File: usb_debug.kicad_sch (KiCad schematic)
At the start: 12 parts, among them J10 DBG pads (SWCLK SWDIO GND), J4 USB_C_PROGRAM_POWER

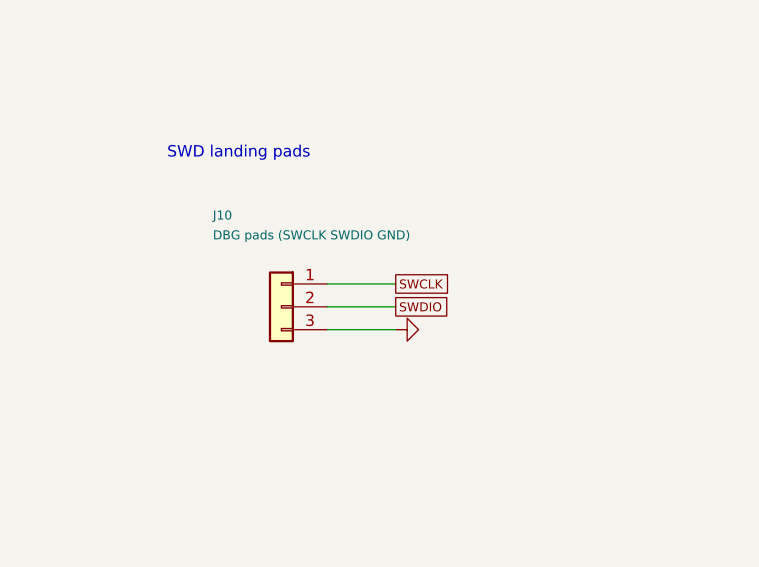
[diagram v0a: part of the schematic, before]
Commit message: Order-ready: core regulator per RP2350 §6.3.8, SWD header, second DVDD cap, README rewrite
Core regulator (U20 / C39 / C45 / L20):
- C39/C45 lands narrowed to 0.46 mm (0.50 mm gap) so VREG_LX passes between
  the pads as in datasheet Fig. 23; local 0.12 mm clearance rule for those
  two footprints only (inside JLC's 3.5 mil four-layer tier)
- In1 GND cutout under L20 and the LX net (Fig. 24); single-point ground
  return with two adjacent vias; B.Cu GND pour tying the SD-cluster vias
- L20 switched to the polarity-marked Abracon AOTA-B201610S3R3-101-T
  (LCSC C42411119) with a silk orientation dot at pad 2 / DVDD
- C81 added: second 4.7 uF on DVDD at the far edge of the package
- U22 BMP581: traces/vias moved out from under the body, mask window opened

Debug: J10 is now a 1x03 2.54 mm THT header wired SWCLK-GND-SWDIO
(Raspberry Pi Debug Probe order); checker, exporter, BOM sources and DFM
rules updated to match.

DFM: courtyard rules relaxed to JLC's body-to-body equivalents (non-overlap
for chip/SOT/SOIC, 0.5 mm courtyard gap IC-to-IC); all 81 findings cleared
without moving parts. DRC 0 errors, 0 unconnected, 0 parity; ERC 0.

Docs: README rewritten around the board, sensor suite, power architecture,
design decisions (external conversion, Q1/D1 OR, sensor LDO, native SD over
PIO, locking microSD socket, fab tier) and the input-power simulation;
DESIGN_SPEC status text brought current; communication-architecture.md
marked historical. Stale root MARV-V2.drl removed (exports live in build/).

Co-Authored-By: Claude Fable 5.1 <noreply@anthropic.com>
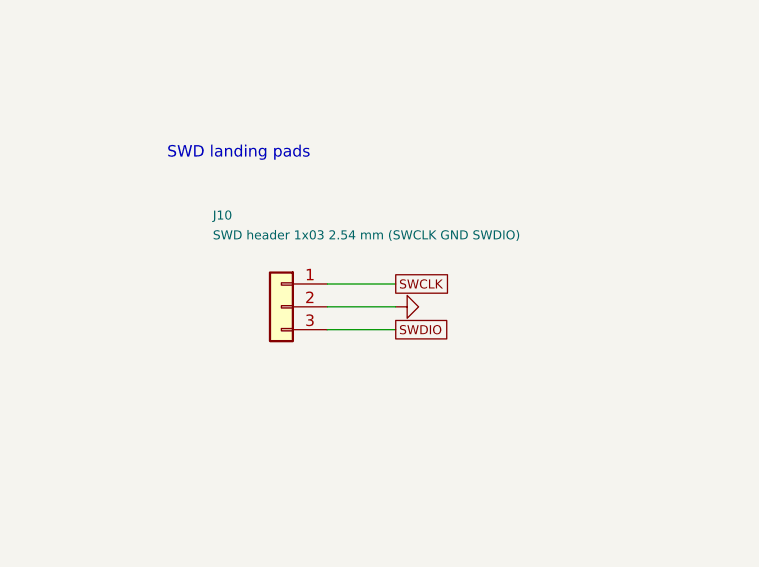
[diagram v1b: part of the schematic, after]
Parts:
- J10: value DBG pads (SWCLK SWDIO GND) -> SWD header 1x03 2.54 mm (SWCLK GND SWDIO); footprint MARV_Packages:PadRow_1x03_P2.00mm -> Connector_PinHeader_2.54mm:PinHeader_1x03_P2.54mm_Vertical
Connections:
- net GND: now also J10.2 (Pin_2); no longer J10.3 (Pin_3)
- net SWDIO: now also J10.3 (Pin_3); no longer J10.2 (Pin_2)
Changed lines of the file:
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@@
 	(global_label "SWDIO"
 		(shape passive)
-		(at 222.25 130.81 0)
+		(at 222.25 133.35 0)
 		(effects
 			(font
@@
 			)
 		)
-		(property "Value" "DBG pads (SWCLK SWDIO GND)"
+		(property "Value" "SWD header 1x03 2.54 mm (SWCLK GND SWDIO)"
 			(at 201.93 122.85 0)
 			(show_name no)
@@
 			)
 		)
-		(property "Footprint" "MARV_Packages:PadRow_1x03_P2.00mm"
+		(property "Footprint" "Connector_PinHeader_2.54mm:PinHeader_1x03_P2.54mm_Vertical"
 			(at 209.55 130.81 0)
 			(hide yes)
@@
 	(symbol
 		(lib_id "power:GND")
-		(at 222.25 133.35 90)
+		(at 222.25 130.81 90)
 		(unit 1)
 		(body_style 1)
@@
 		(dnp no)
 		(property "Reference" "#PWR041"
-			(at 222.25 127.68 270)
+			(at 222.25 125.14 270)
 			(hide yes)
 			(show_name no)
@@
 		)
 		(property "Value" "GND"
-			(at 222.25 129.88 270)
+			(at 222.25 127.34 270)
 			(hide yes)
 			(show_name no)
@@
 		)
 		(property "Footprint" ""
-			(at 222.25 133.35 270)
-			(hide yes)
-			(show_name no)
-			(do_not_autoplace no)
-			(effects
-				(font
-					(size 1 1)
-				)
-				(justify left)
-			)
-		)
-		(property "Datasheet" ""
-			(at 222.25 133.35 270)
-			(hide yes)
-			(show_name no)
-			(do_not_autoplace no)
-			(effects
-				(font
-					(size 1 1)
-				)
-				(justify left)
-			)
-		)
-		(property "Description" ""
-			(at 222.25 133.35 0)
-			(show_name no)
-			(do_not_autoplace no)
+			(at 222.25 130.81 270)
+			(hide yes)
+			(show_name no)
+			(do_not_autoplace no)
+			(effects
+				(font
+					(size 1 1)
+				)
+				(justify left)
+			)
+		)
+		(property "Datasheet" ""
+			(at 222.25 130.81 270)
+			(hide yes)
+			(show_name no)
+			(do_not_autoplace no)
+			(effects
+				(font
+					(size 1 1)
+				)
+				(justify left)
+			)
+		)
+		(property "Description" ""
+			(at 222.25 130.81 0)
+			(show_name no)
+			(do_not_autoplace no)

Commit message: Move JLCPCB export to Fabrication Toolkit; drop tools/jlc scripts
- Add fabrication-toolkit-options.json (auto translate + exclude DNP on;
  auto fill, V-cut, alternate outline, all-active-layer plotting off)
- Mark hand-soldered headers and board-only footprints excluded from
  BOM/position files in both schematic and PCB (U24 stays DNP)
- Remove tools/jlc/*, tools/jlc/lcsc_map.csv and power_bom.csv;
  the plugin now produces production/{MARV-V2.zip,bom.csv,positions.csv}
- Ignore generated production/ output; update README and LIBRARIES.md

Verified: 88 top-side placements, 34 LCSC parts, XY identical to prior
export; ERC 0, DRC 0 errors / 0 unconnected / 0 parity issues.

Co-Authored-By: Claude Fable 5.1 <noreply@anthropic.com>
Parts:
- J10: now left out of the parts list
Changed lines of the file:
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@@
 		(body_style 1)
 		(exclude_from_sim no)
-		(in_bom yes)
+		(in_bom no)
 		(on_board yes)
-		(in_pos_files yes)
+		(in_pos_files no)
 		(dnp no)
 		(property "Reference" "J10"
